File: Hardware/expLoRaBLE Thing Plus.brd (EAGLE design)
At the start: 22.9 x 58.4 mm, 143 parts, among them J2 CORTEX_DEBUG, J5 USB-C, J8 U.FL, U1 MCP73831, U2 3.3V, U3 NM180100, U4 CH340E_MSOP10, U6 DPX202700DT-4162A1, Y1 32.768kHz

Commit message: RTS jumper buzzard label
-renamed jumper to "RTS"
-added buzzard label
-also moved user silk "10" to new button position
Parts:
- added U$24: (no value), output:#RTS#0
- moved U$97 11.8 mm to (9.35, 13.7)
- renumbered JP1 to RTS
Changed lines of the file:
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@@
 <drawing>
 <settings>
-<setting alwaysvectorfont="no"/>
+<setting alwaysvectorfont="yes"/>
 <setting verticaltext="up"/>
 </settings>
-<grid distance="0.001" unitdist="inch" unit="inch" style="lines" multiple="1" display="yes" altdistance="0.001" altunitdist="inch" altunit="inch"/>
+<grid distance="0.05" unitdist="inch" unit="inch" style="lines" multiple="1" display="yes" altdistance="0.005" altunitdist="inch" altunit="inch"/>
 <layers>
-<layer number="1" name="Top" color="4" fill="1" visible="no" active="yes"/>
+<layer number="1" name="Top" color="4" fill="1" visible="yes" active="yes"/>
 <layer number="2" name="Route2" color="11" fill="3" visible="no" active="yes"/>
 <layer number="3" name="Route3" color="17" fill="1" visible="no" active="no"/>
@@
 <layer number="13" name="Route13" color="21" fill="1" visible="no" active="no"/>
 <layer number="14" name="Route14" color="22" fill="1" visible="no" active="no"/>
-<layer number="15" name="Route15" color="13" fill="6" visible="yes" active="yes"/>
+<layer number="15" name="Route15" color="13" fill="6" visible="no" active="yes"/>
 <layer number="16" name="Bottom" color="1" fill="1" visible="yes" active="yes"/>
 <layer number="17" name="Pads" color="2" fill="1" visible="yes" active="yes"/>
@@
 </layers>
 <board>
-<fusionsync huburn="a.YnVzaW5lc3M6Z21haWwxMTI2MzE1" projecturn="a.YnVzaW5lc3M6Z21haWwxMTI2MzE1I0QyMDIwMDgzMTMyODE1ODgwNg" f3durn="urn:adsk.wipprod:dm.lineage:mHH6g35GTyuWC89OADwm_A" pcbguid="" lastpulledtime="" lastsyncedchangeguid="" latestrevisionid="c9279973-d255-4697-9a7c-0f6c20acbc86" lastsyncedrevisionid="c9279973-d255-4697-9a7c-0f6c20acbc86" lastboardhashguid="e8377822-6ace-51a9-b550-49c57cccff0e" lastpushedtime="2020-10-21T19:52:57Z" linktopcb3d="true"/>
+<fusionsync huburn="a.YnVzaW5lc3M6Z21haWwxMTI2MzE1" projecturn="a.YnVzaW5lc3M6Z21haWwxMTI2MzE1I0QyMDIwMDgzMTMyODE1ODgwNg" f3durn="urn:adsk.wipprod:dm.lineage:mHH6g35GTyuWC89OADwm_A" pcbguid="" lastpulledtime="" lastsyncedchangeguid="" latestrevisionid="c9279973-d255-4697-9a7c-0f6c20acbc86" lastsyncedrevisionid="c9279973-d255-4697-9a7c-0f6c20acbc86" lastboardhashguid="e8377822-6ace-51a9-b550-49c57cccff0e" lastpushedtime="2020-10-21T19:52:57Z" linktopcb3d="false"/>
 <plain>
 <wire x1="0" y1="55.88" x2="0" y2="2.54" width="0.2032" layer="20"/>
@@
 <element name="U$95" library="output" package="#RST#0" value="" x="19.3548" y="13.9192" smashed="yes"/>
 <element name="U$96" library="output" package="RST0" value="" x="18.1864" y="10.414" smashed="yes" rot="R90"/>
-<element name="U$97" library="output" package="100" value="" x="16.7132" y="22.9616" smashed="yes"/>
+<element name="U$97" library="output" package="100" value="" x="9.3472" y="13.6906" smashed="yes"/>
 <element name="U$98" library="output" package="#0" value="" x="10.414" y="15.875" smashed="yes"/>
 <element name="U$99" library="output" package="#_0" value="" x="10.668" y="19.9644" smashed="yes"/>
@@
 <attribute name="VALUE" x="17.3228" y="25.4762" size="0.6096" layer="27" font="vector" ratio="20" rot="R270" align="top-center"/>
 </element>
-<element name="JP1" library="SparkFun-Jumpers" library_urn="urn:adsk.eagle:library:528" package="SMT-JUMPER_2_NO_SILK" package3d_urn="urn:adsk.eagle:package:39279/1" value="JUMPER-SMT_2_NO_SILK" x="15.24" y="21.59" smashed="yes" rot="MR270">
+<element name="RTS" library="SparkFun-Jumpers" library_urn="urn:adsk.eagle:library:528" package="SMT-JUMPER_2_NO_SILK" package3d_urn="urn:adsk.eagle:package:39279/1" value="JUMPER-SMT_2_NO_SILK" x="15.24" y="21.59" smashed="yes" rot="MR270">
 <attribute name="NAME" x="14.097" y="21.59" size="0.6096" layer="26" font="vector" ratio="20" rot="MR270" align="bottom-center"/>
 <attribute name="VALUE" x="16.383" y="21.59" size="0.6096" layer="28" font="vector" ratio="20" rot="MR270" align="top-center"/>
 </element>
+<element name="U$24" library="output" package="#RTS#0" value="" x="15.24" y="20.828" smashed="yes" rot="MR90"/>
 </elements>
 <signals>
@@
 <wire x1="16.8656" y1="13.97" x2="16.8402" y2="13.9954" width="0.2032" layer="16"/>
 <via x="16.8402" y="13.9954" extent="1-16" drill="0.3048"/>
-<contactref element="JP1" pad="2"/>
+<contactref element="RTS" pad="2"/>
 <wire x1="16.8402" y1="19.0246" x2="15.24" y2="20.6248" width="0.2032" layer="16"/>
 <wire x1="15.24" y1="21.1836" x2="15.24" y2="20.6248" width="0.2032" layer="16"/>
@@
 <signal name="N$15">
 <contactref element="C1" pad="2"/>
-<contactref element="JP1" pad="1"/>
+<contactref element="RTS" pad="1"/>
 <wire x1="15.24" y1="21.9964" x2="15.24" y2="23.6474" width="0.2032" layer="16"/>
 <via x="16.2052" y="24.6126" extent="1-16" drill="0.3048"/>

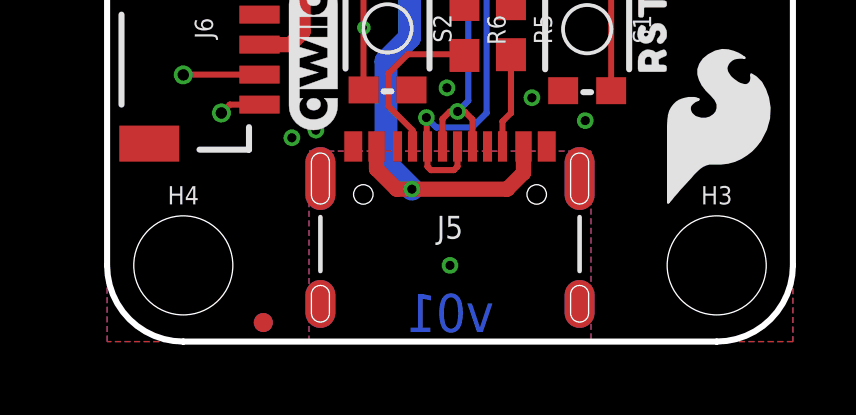
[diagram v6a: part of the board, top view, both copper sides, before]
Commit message: Fixed short from 3.3V to GND caused by USB connector mill holes
Adjusted inner layer polygons to not pour under the USB connector. Previously these were shorting all planes together, causing a short between 3.3V NET and GND NET.
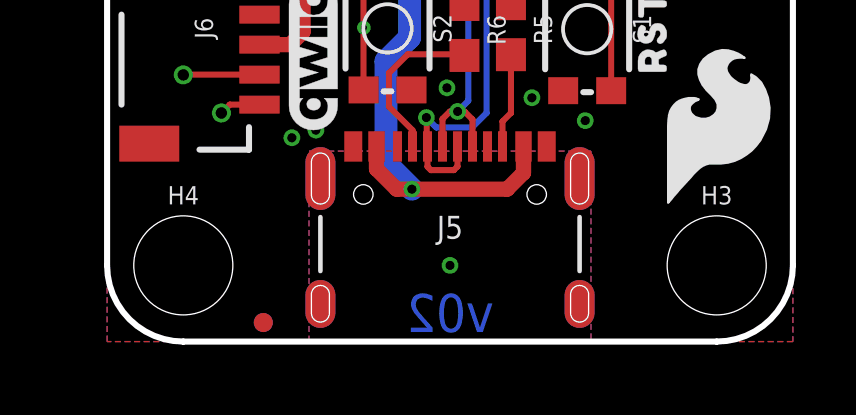
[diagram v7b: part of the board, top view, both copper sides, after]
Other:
- board text added: "v02"
- board text removed: "v01"
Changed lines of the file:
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@@
 <drawing>
 <settings>
-<setting alwaysvectorfont="yes"/>
+<setting alwaysvectorfont="no"/>
 <setting verticaltext="up"/>
 </settings>
@@
 <layers>
 <layer number="1" name="Top" color="4" fill="1" visible="yes" active="yes"/>
-<layer number="2" name="Route2" color="11" fill="3" visible="no" active="yes"/>
+<layer number="2" name="Route2" color="11" fill="3" visible="yes" active="yes"/>
 <layer number="3" name="Route3" color="17" fill="1" visible="no" active="no"/>
 <layer number="4" name="Route4" color="18" fill="1" visible="no" active="no"/>
@@
 <layer number="13" name="Route13" color="21" fill="1" visible="no" active="no"/>
 <layer number="14" name="Route14" color="22" fill="1" visible="no" active="no"/>
-<layer number="15" name="Route15" color="13" fill="6" visible="no" active="yes"/>
+<layer number="15" name="Route15" color="13" fill="6" visible="yes" active="yes"/>
 <layer number="16" name="Bottom" color="1" fill="1" visible="yes" active="yes"/>
 <layer number="17" name="Pads" color="2" fill="1" visible="yes" active="yes"/>
@@
 <dimension x1="0" y1="2.54" x2="22.86" y2="2.54" x3="11.43" y3="-8.89" textsize="1.27" layer="47" unit="inch" visible="yes"/>
 <dimension x1="2.54" y1="0" x2="2.54" y2="58.42" x3="-8.89" y3="29.21" textsize="1.27" layer="47" unit="inch"/>
-<text x="11.43" y="0.3175" size="1.27" layer="16" font="vector" ratio="15" rot="MR0" align="bottom-center">v01</text>
+<text x="11.43" y="0.3175" size="1.27" layer="16" font="vector" ratio="15" rot="MR0" align="bottom-center">v02</text>
 <text x="-30.48" y="-39.37" size="5.08" layer="51" font="vector">4-LAYER BOARD</text>
 <text x="0.635" y="17.78" size="0.8128" layer="1" font="vector" ratio="25">1</text>
@@
 <vertex x="22.86" y="58.42"/>
 <vertex x="22.86" y="0"/>
+<vertex x="16.891" y="0"/>
+<vertex x="16.891" y="6.985"/>
+<vertex x="6.096" y="6.985"/>
+<vertex x="6.096" y="0"/>
 <vertex x="0" y="0"/>
 </polygon>
@@
 <vertex x="22.86" y="44.45"/>
 <vertex x="22.86" y="0"/>
+<vertex x="16.891" y="0"/>
+<vertex x="16.891" y="6.985"/>
+<vertex x="6.096" y="6.985"/>
+<vertex x="6.096" y="0"/>
 </polygon>
 <wire x1="6.8834" y1="42.4716" x2="6.1981" y2="43.1569" width="0.1524" layer="1"/>

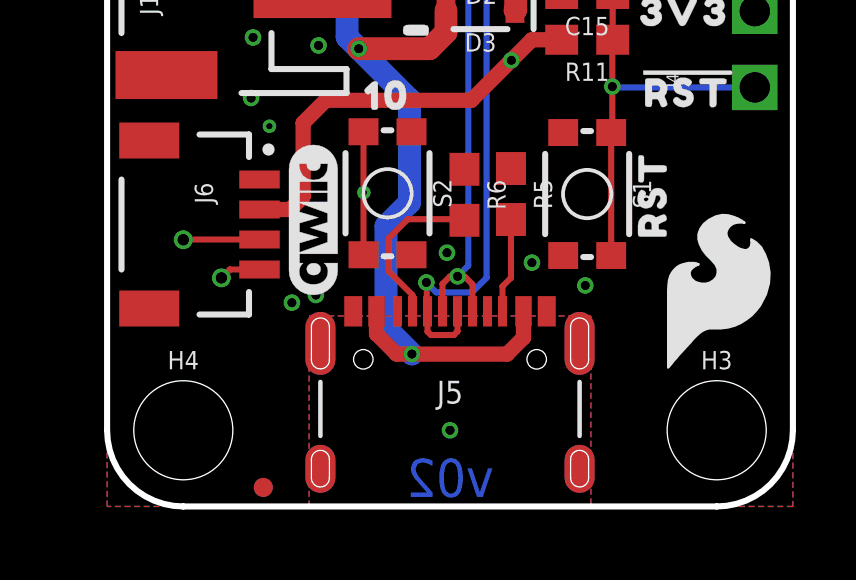
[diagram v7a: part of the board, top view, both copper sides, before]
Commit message: Updating to USB-C-16P-4-LAYER-ISOLATED
-This new footprint includes the isolation (aka cutout polygons). It is better to include these at the library lavel (rather than in the board, as it was previously).

-Note, had to re-route VBUS, because the update also included moving the pads south to match the datasheet. This update commit history to the connector library here: https://github.com/sparkfun/SparkFun-Eagle-Libraries/commit/385c00bb90b92dfd747075cffe71177065b70510#diff-c73d36e753812bf738f1d00b48f2ac4ee18b59eb919db6021d587bb22fbbb9cd
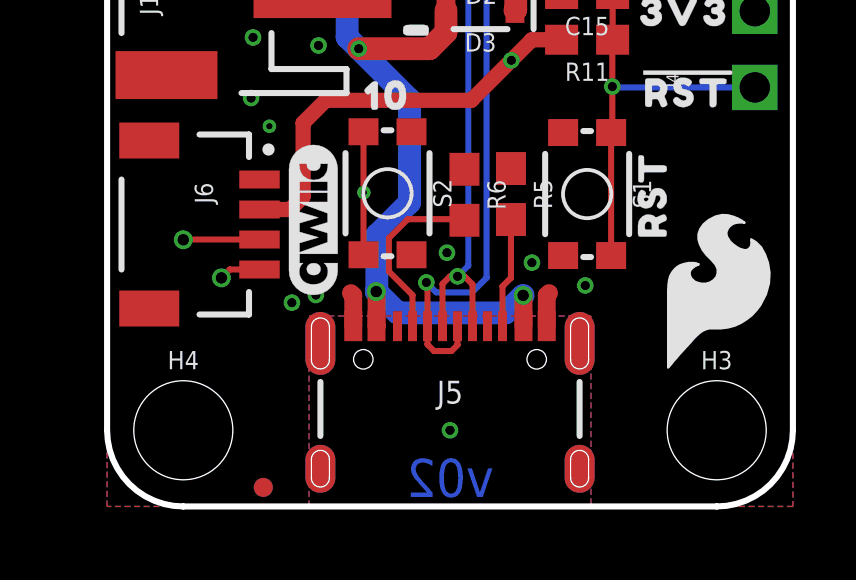
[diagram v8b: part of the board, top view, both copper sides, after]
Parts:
- J5: value USB-C -> USB Female Type C Connector; device SparkFun-Connectors:USB-C-16P -> SparkFun-Connectors:USB-C-16P-4LAYER-ISOLATED
- J6: value (none) -> QWIIC_RIGHT_ANGLE
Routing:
- net GND: track 0.98 -> 3.25 mm
- net V_USB: track 57.0 -> 55.3 mm, vias 5 -> 6
- net D+1: track 30.1 -> 31.1 mm
